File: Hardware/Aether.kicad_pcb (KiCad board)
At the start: 2 copper layers, 10 parts, among them Q1 BSS84, U1 VENUS838LPX-L

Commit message: Radio schematic and rough layout
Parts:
- added C10: C, CAPC1608-N, F.Cu at (294.5, 66.0)
- added C11: C, CAPC1608-N, F.Cu at (277.5, 74.5)
- added C12: C, CAPC1608-N, F.Cu at (277.5, 72.5)
- added C4: 33pF, CAPC1608-N, F.Cu at (292.5, 86.0)
- added C5: 0.1uF, CAPC1608-N, F.Cu at (285.0, 63.0)
- added C6: 100pF, CAPC1608-N, F.Cu at (292.5, 88.0)
- added C7: 0.1uF, CAPC1608-N, F.Cu at (298.0, 78.0)
- added C8: 2.2uF, CAPC1608-N, F.Cu at (294.0, 84.0)
- added C9: 0.1uF, CAPC1608-N, F.Cu at (298.0, 80.5)
- added FB1: FERRITE, INDC1608-N, F.Cu at (298.0, 83.0)
- added L2: L, INDC1608-N, F.Cu at (280.0, 73.5)
- added Q2: BSS84, SOT95P280-3N-GDS, F.Cu at (280.5, 66.0)
- added R4: R, RESC1608-N, F.Cu at (288.5, 66.0)
- added R5: R, RESC1608-N, F.Cu at (290.5, 66.0)
- added R6: R, RESC1608-N, F.Cu at (292.5, 66.0)
- added R7: 10k, RESC1608-N, F.Cu at (280.5, 63.0)
- added R8: 10k, RESC1608-N, F.Cu at (277.5, 70.5)
- added U2: SI4464, QFN50P400X400-21N, F.Cu at (286.0, 73.5)
- added X1: 27MHz, OSCCC320X250-N, F.Cu at (285.0, 66.0)

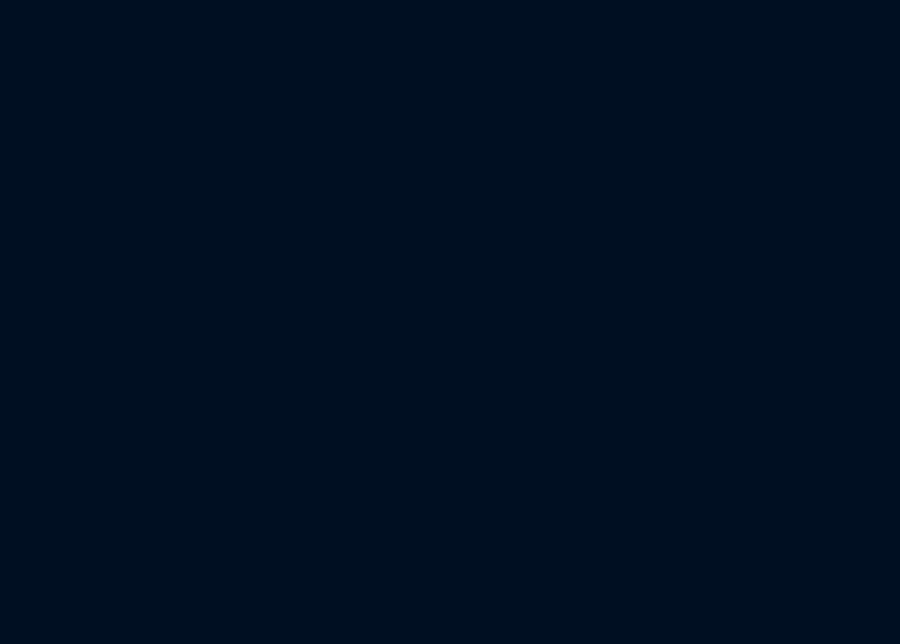
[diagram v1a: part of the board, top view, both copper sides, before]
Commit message: 5v regulator schematic and rough layout
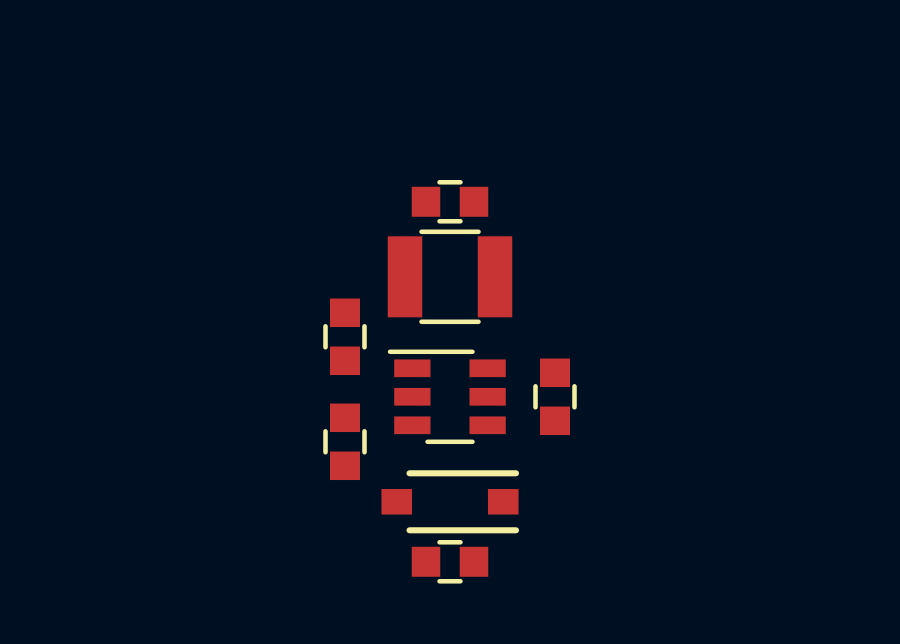
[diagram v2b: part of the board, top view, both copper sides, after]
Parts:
- added C13: 10uF, CAPC1608-N, F.Cu at (267.5, 112.0)
- added C14: 10uF, CAPC1608-N, F.Cu at (267.5, 124.0)
- added D1: MBR0520L, SOD3716-N, F.Cu at (267.5, 122.0)
- added L3: 4.7uH, INDC3225-N, F.Cu at (267.5, 114.5)
- added R10: 30k, RESC1608-N, F.Cu at (264.0, 120.0)
- added R11: 10k, RESC1608-N, F.Cu at (264.0, 116.5)
- added R9: 10k, RESC1608-N, F.Cu at (271.0, 118.5)
- added U3: AAT1217, SOT95P280-6N, F.Cu at (267.5, 118.5)
- R2: value 10k -> 30k
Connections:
- C1 pad 1: N-0000021 -> N-0000022
- C2 pad 1: N-0000023 -> N-0000024
- Q1 pad D: N-0000023 -> N-0000024
- R2 pad 1: N-0000021 -> N-0000024
- R2 pad 2: N-0000023 -> N-0000022
- R3 pad 1: N-0000023 -> N-0000024
- U1 pad 1: N-0000021 -> N-0000022
- U1 pad 2: N-0000023 -> N-0000024
- U1 pad 36: N-0000023 -> N-0000024
- U1 pad 8: N-0000023 -> N-0000024
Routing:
- net N-0000023: track 17.2 -> 0.00 mm
- net N-0000024: track 0.00 -> 16.6 mm
- net N-0000022: track 0.00 -> 4.96 mm
- net N-0000021: track 4.36 -> 0.00 mm

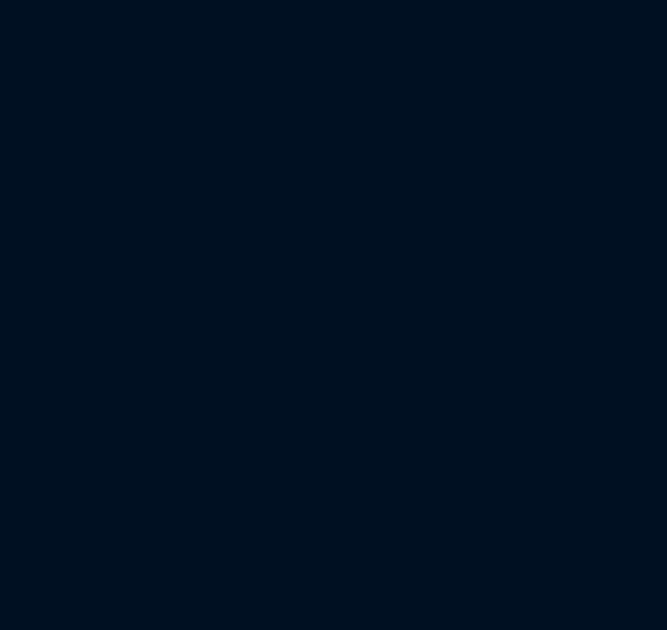
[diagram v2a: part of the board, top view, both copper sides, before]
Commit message: 3v3 regulator schematic and rough layout
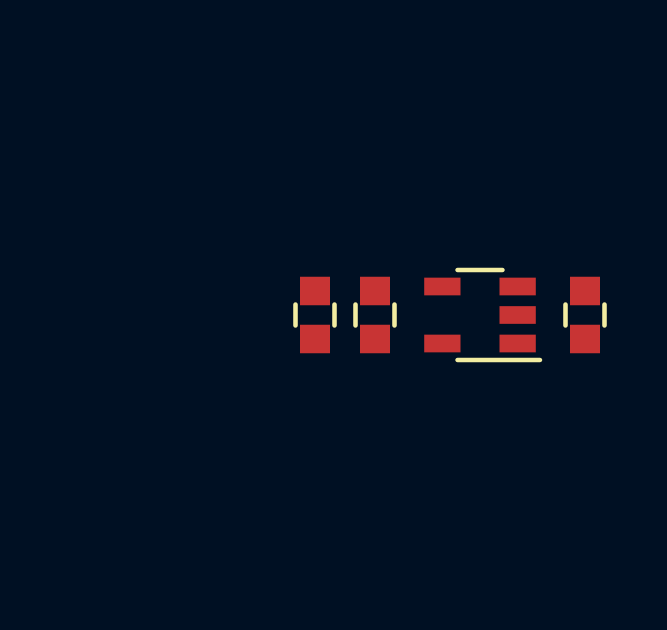
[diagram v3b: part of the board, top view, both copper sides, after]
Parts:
- added C15: 10uF, CAPC1608-N, F.Cu at (299.5, 113.5)
- added C16: 10uF, CAPC1608-N, F.Cu at (290.5, 113.5)
- added L4: 2.2uh, INDC1608-N, F.Cu at (292.5, 113.5)
- added U4: LM3671, SOT95P280-5N, F.Cu at (296.0, 113.5)
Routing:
- net N-0000023: track 16.6 -> 10.5 mm
- net N-0000021: track 4.96 -> 11.0 mm

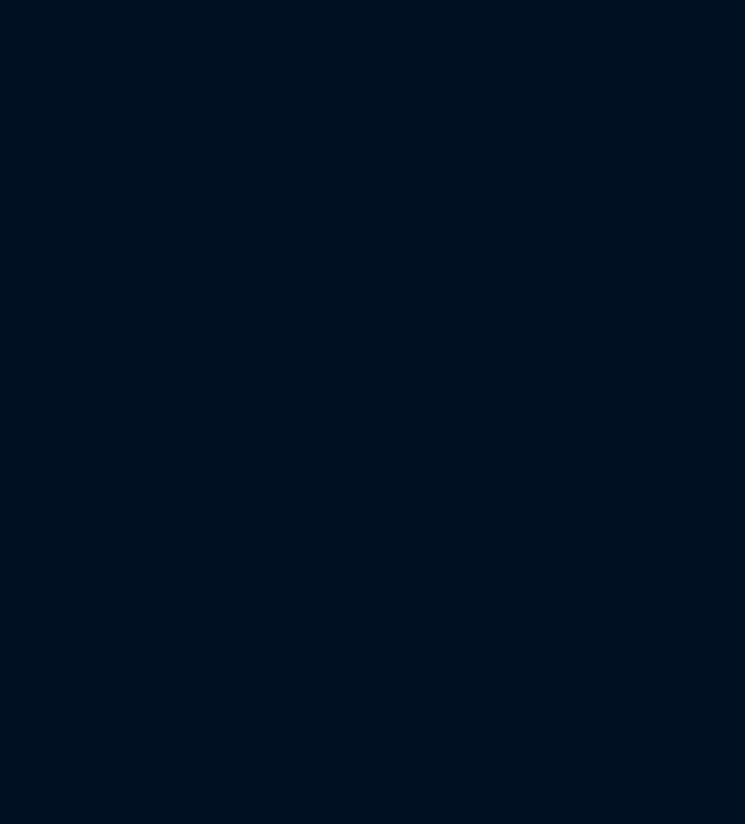
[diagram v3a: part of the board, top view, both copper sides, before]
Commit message: Add charger and batteries to schematic and board
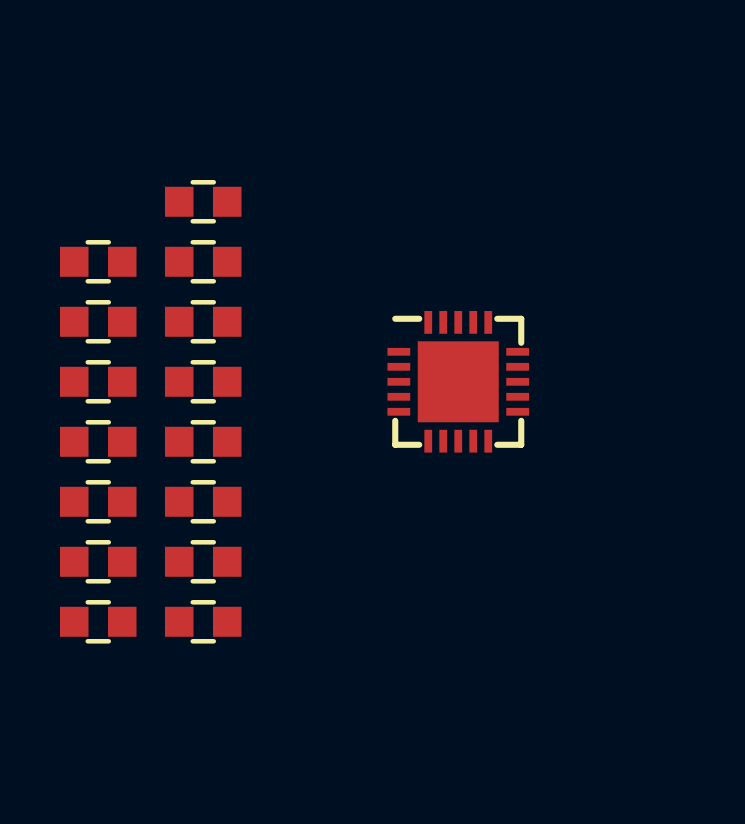
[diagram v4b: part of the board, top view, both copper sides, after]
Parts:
- added C17: 10uF, CAPC1608-N, F.Cu at (213.0, 114.0)
- added C18: 10uF, CAPC1608-N, F.Cu at (213.0, 120.0)
- added C19: 10uF, CAPC1608-N, F.Cu at (209.5, 120.0)
- added R12: R, RESC1608-N, F.Cu at (209.5, 116.0)
- added R13: R, RESC1608-N, F.Cu at (209.5, 114.0)
- added R14: 10k, RESC1608-N, F.Cu at (209.5, 112.0)
- added R15: 10k, RESC1608-N, F.Cu at (209.5, 110.0)
- added R16: 10k, RESC1608-N, F.Cu at (213.0, 118.0)
- added R17: 10k, RESC1608-N, F.Cu at (213.0, 110.0)
- added R18: R, RESC1608-N, F.Cu at (213.0, 112.0)
- added R19: R, RESC1608-N, F.Cu at (213.0, 116.0)
- added R20: 10k, RESC1608-N, F.Cu at (213.0, 106.0)
- added R21: 10k, RESC1608-N, F.Cu at (213.0, 108.0)
- added R22: 10k, RESC1608-N, F.Cu at (209.5, 108.0)
- added TH1: 10k, RESC1608-N, F.Cu at (209.5, 118.0)
- added U5: MCP73871, QFN50P400X400-21N, F.Cu at (221.5, 112.0)
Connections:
- net VCOM renamed +5V

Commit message: Core support circuitry
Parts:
- added C20: 0.1uF, CAPC1608-N, F.Cu at (332.0, 95.5)
- added C21: 1uF, CAPC1608-N, F.Cu at (330.0, 95.5)
- added C22: C, CAPC1608-N, F.Cu at (326.0, 90.0)
- added C23: 10uF, CAPC1608-N, F.Cu at (337.0, 103.5)
- added C24: C, CAPC1608-N, F.Cu at (328.0, 90.0)
- added C25: 0.1uF, CAPC1608-N, F.Cu at (337.0, 101.5)
- added C26: 0.1uF, CAPC1608-N, F.Cu at (326.0, 95.5)
- added C27: 0.1uF, CAPC1608-N, F.Cu at (343.5, 101.5)
- added C28: 0.1uF, CAPC1608-N, F.Cu at (348.0, 90.0)
- added C29: 0.1uF, CAPC1608-N, F.Cu at (336.5, 85.5)
- added C30: 0.1uF, CAPC1608-N, F.Cu at (332.0, 90.0)
- added FB2: FERRITE, INDC1608-N, F.Cu at (328.0, 95.5)
- added J1: ICSP-CORTEX, CONN-TC-2030-NL, F.Cu at (365.0, 72.0)
- added R23: 10k, RESC1608-N, F.Cu at (336.5, 83.5)
- added R24: 10k, RESC1608-N, F.Cu at (330.0, 90.0)
- added U6: STM32L100RBT6, QFP50P1200X1200-64N, F.Cu at (340.0, 93.5)

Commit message: Add usb
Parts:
- added J2: USB_MINI, CONN-USB-M26FTR, F.Cu at (354.5, 75.0)
- moved C10 96.9 mm to (388.5, 89.5)
- moved C11 96.9 mm to (371.5, 98.0)
- moved C12 96.9 mm to (371.5, 96.0)
- moved C5 96.9 mm to (379.0, 86.5)
- moved L2 96.9 mm to (374.0, 97.0)
- moved Q2 96.9 mm to (374.5, 89.5)
- moved R4 96.9 mm to (382.5, 89.5)
- moved R5 96.9 mm to (384.5, 89.5)
- moved R6 96.9 mm to (386.5, 89.5)
- moved R7 96.9 mm to (374.5, 86.5)
- moved R8 96.9 mm to (371.5, 94.0)
- moved U2 96.9 mm to (380.0, 97.0)
- moved X1 96.9 mm to (379.0, 89.5)
- moved C4 92.9 mm to (383.5, 104.5)
- moved C6 92.9 mm to (383.5, 106.5)
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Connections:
- net /Radio/XCVR_SDN renamed /Core/XCVR_SDN
- U2 pad 12: (no net) -> /Core/XCVR_SCLK
- U2 pad 13: (no net) -> /Core/XCVR_MISO
- U2 pad 14: (no net) -> /Core/XCVR_MOSI
- U2 pad 15: (no net) -> /Core/~XCVR_SEL
- U6 pad 33: (no net) -> /Core/~XCVR_SEL
- U6 pad 34: (no net) -> /Core/XCVR_SCLK
- U6 pad 35: (no net) -> /Core/XCVR_MISO
- U6 pad 36: (no net) -> /Core/XCVR_MOSI
- U6 pad 44: (no net) -> /Core/USB_DM
- U6 pad 45: (no net) -> /Core/USB_DP

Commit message: Connect subsystems
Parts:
- moved U2 17.0 mm to (363.0, 96.0), turned to 180 degrees
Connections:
- Q1 pad G: /GPS/GPS_EN -> /Core/GPS_EN
- Q2 pad G: /Radio/LO_EN -> /Core/LO_EN
- R1 pad 1: /GPS/GPS_EN -> /Core/GPS_EN
- R7 pad 1: /Radio/LO_EN -> /Core/LO_EN
- U1 pad 42: (no net) -> /Core/GPS_MOSI
- U1 pad 44: (no net) -> /Core/GPS_MISO
- U2 pad 11: (no net) -> /Core/~XCVR_INT
- U6 pad 15: (no net) -> /Core/GPS_EN
- U6 pad 16: (no net) -> /Core/GPS_MOSI
- U6 pad 17: (no net) -> /Core/GPS_MISO
- U6 pad 20: (no net) -> /Core/LO_EN
- U6 pad 21: (no net) -> /Core/LO_MOD
- U6 pad 37: (no net) -> /Core/~XCVR_INT
- X1 pad 1: (no net) -> /Core/LO_MOD
